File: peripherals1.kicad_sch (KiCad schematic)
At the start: 33 parts, among them Q1 Q_NMOS_GSD, SW3 SW_Push, SW4 SW_Push, SW5 SW_Push, SW6 SW_Push, SW7 SW_Push, SW8 SW_Push, U7 TSDP343xx

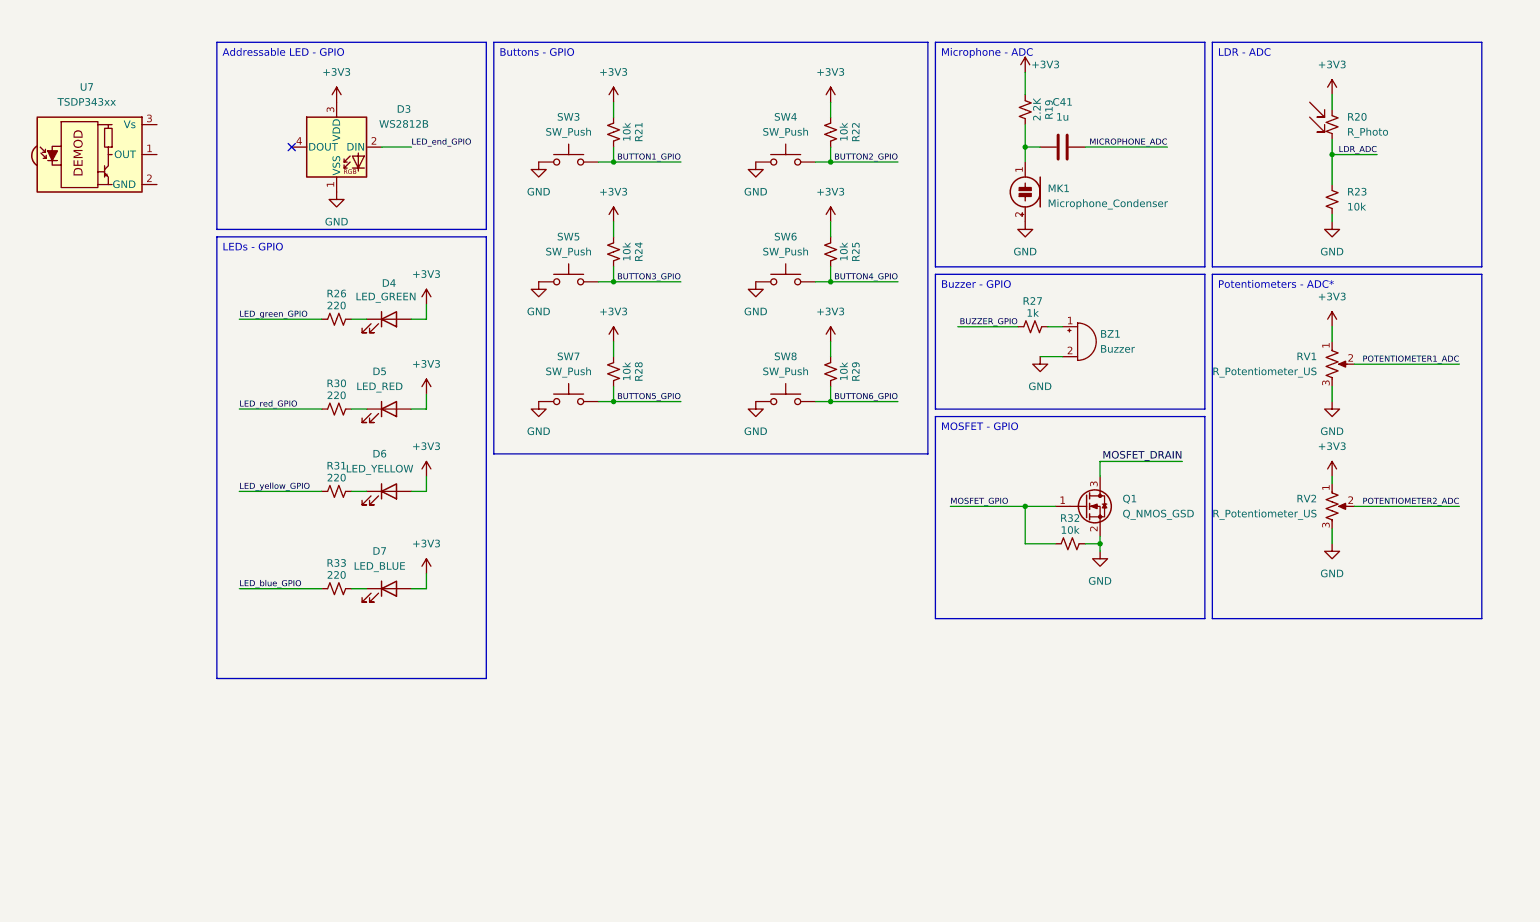
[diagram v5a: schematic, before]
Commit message: chore: links global labels
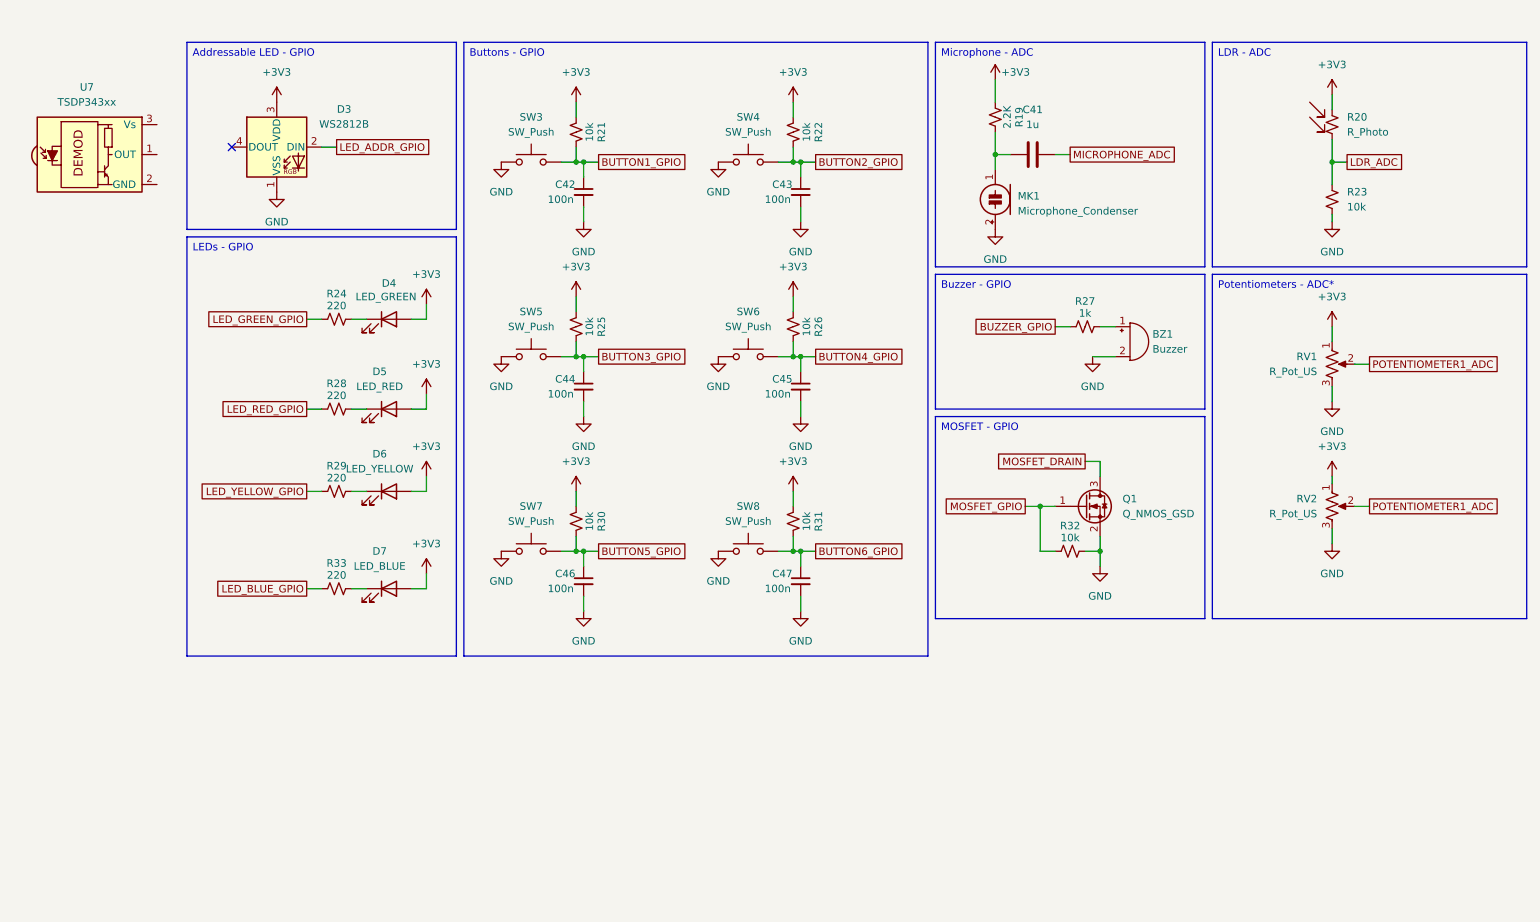
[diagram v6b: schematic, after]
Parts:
- added C42, C43, C44, C45, C46, C47: 100n, Capacitor_SMD:C_0402_1005Metric, symbol Device:C_Small
- RV1, RV2: value R_Potentiometer_US -> R_Pot_US
- renumbered R26 to R24, R24 to R25, R25 to R26, R30 to R28, R31 to R29, R28 to R30, R29 to R31
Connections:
- net POTENTIOMETER2_ADC is gone; now on net POTENTIOMETER1_ADC: RV2.2
- net BUTTON1_GPIO: now also C42.1
- net BUTTON2_GPIO: now also C43.1
- net BUTTON3_GPIO: now also C44.1
- net BUTTON4_GPIO: now also C45.1
- net BUTTON5_GPIO: now also C46.1
- net BUTTON6_GPIO: now also C47.1
- net GND: now also C42.2, C43.2, C44.2, C45.2, C46.2, C47.2
- net LED_blue_GPIO renamed LED_BLUE_GPIO
- net LED_end_GPIO renamed LED_ADDR_GPIO
- net LED_green_GPIO renamed LED_GREEN_GPIO
- net LED_red_GPIO renamed LED_RED_GPIO
- net LED_yellow_GPIO renamed LED_YELLOW_GPIO
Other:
- moved on the sheet: BZ1, C41, D3, MK1, R19, R21, R22, R25, R26, R27, R30, R31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

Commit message: chore: adds titles to sheets and organizes root
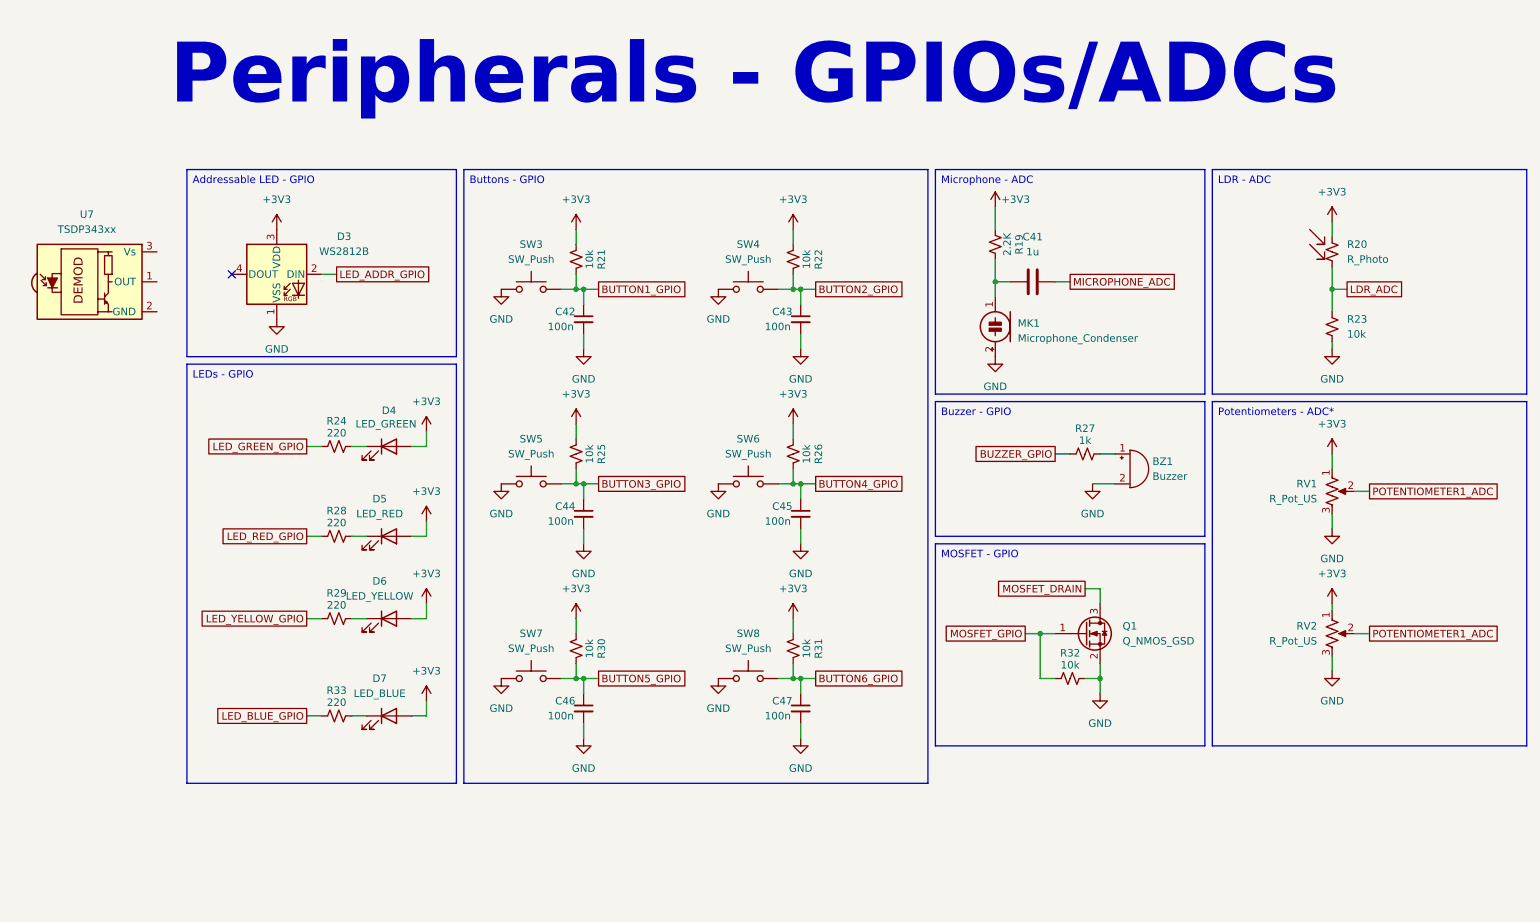
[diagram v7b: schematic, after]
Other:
- note added: "Peripherals - GPIOs/ADCs"
- company: (none) -> Os Circuitados
- title: (none) -> Peripherals - GPIOs and ADCs
- moved on the sheet: BZ1, C41, C42, C43, C44, C45, C46, C47, D3, D4, D5, D6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

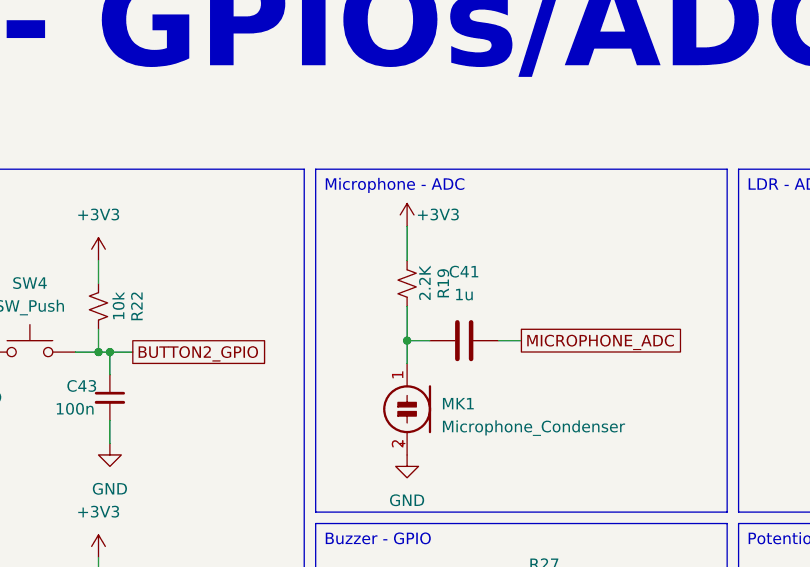
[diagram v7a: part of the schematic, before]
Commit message: refac: standardizes schematic sectorization
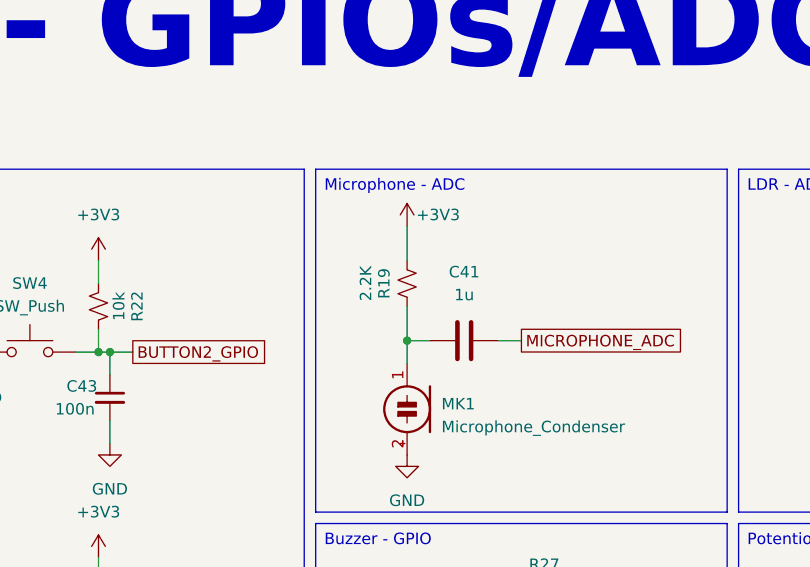
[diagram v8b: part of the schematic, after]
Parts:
- R20: MPN FZ2812-5050 -> PDV-P8103
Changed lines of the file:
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@@
 			)
 		)
-		(property "Datasheet" "https://www.digikey.com.br/en/products/detail/feztek/FZ2812-5050/18647407?s=N4IgTCBcDaIGIC0wA4CMYC0BWADLkAugL5A"
+		(property "Datasheet" "https://www.digikey.com.br/en/products/detail/advanced-photonix/PDV-P8103/480610?s=N4IgTCBcDaIAoBEBqBaOAOAjABgMwgF0BfIA"
 			(at 248.92 52.07 0)
 			(effects
@@
 			)
 		)
-		(property "MPN" "FZ2812-5050"
+		(property "MPN" "PDV-P8103"
 			(at 248.92 52.07 0)
 			(effects
@@
 		(dnp no)
 		(property "Reference" "R19"
-			(at 195.834 50.8 90)
+			(at 189.23 50.8 90)
 			(effects
 				(font
@@
 		)
 		(property "Value" "2.2K"
-			(at 193.802 50.8 90)
-			(effects
-				(font
+			(at 187.198 50.8 90)
+			(effects
+				(font
